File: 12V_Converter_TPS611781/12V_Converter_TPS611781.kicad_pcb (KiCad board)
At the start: 2 copper layers, 40.3 x 28.4 mm, 25 parts, among them M1 IQE050N08NM5CGSC, U1 LM51561HPWPR

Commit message: fix GND side of current sense probe and DRC issues
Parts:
- moved Cvcc1 0.06 mm to (77.8, 108.7)
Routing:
- net GND: track 58.7 -> 67.9 mm

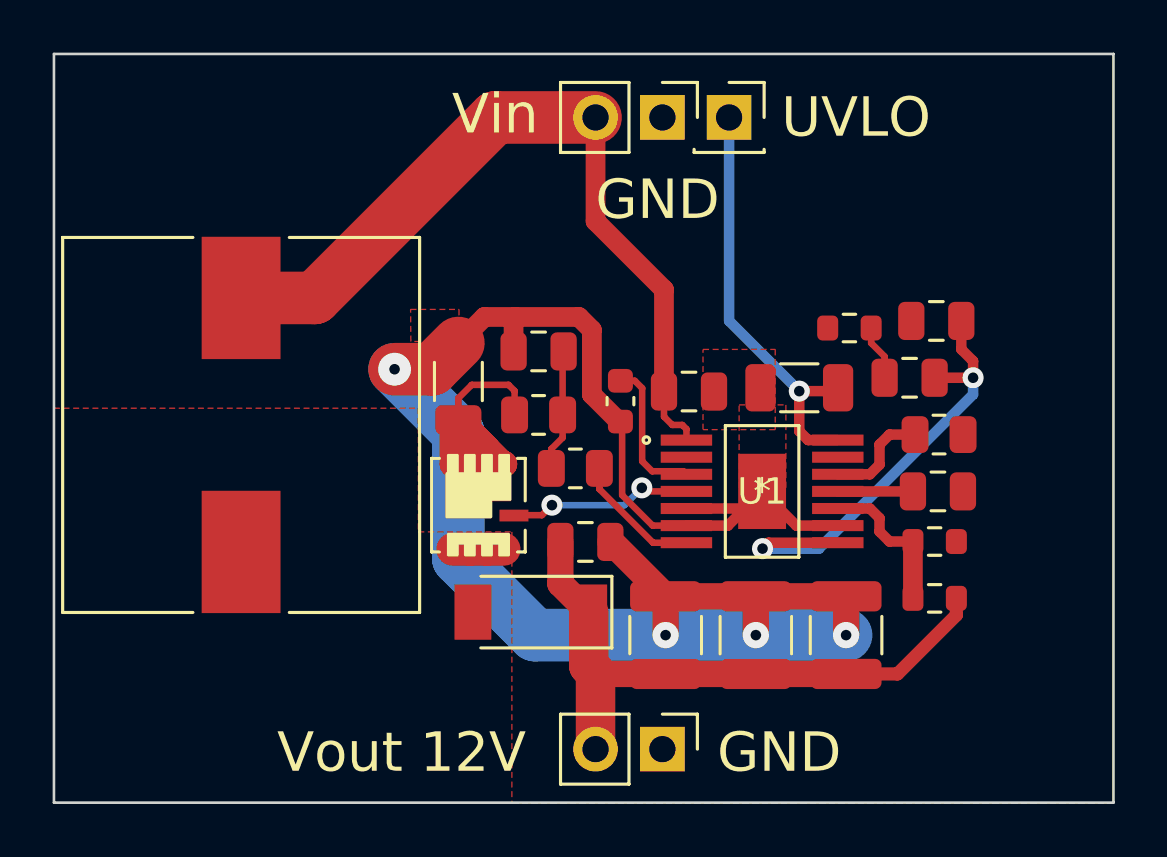
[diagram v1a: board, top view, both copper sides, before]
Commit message: improve thermals
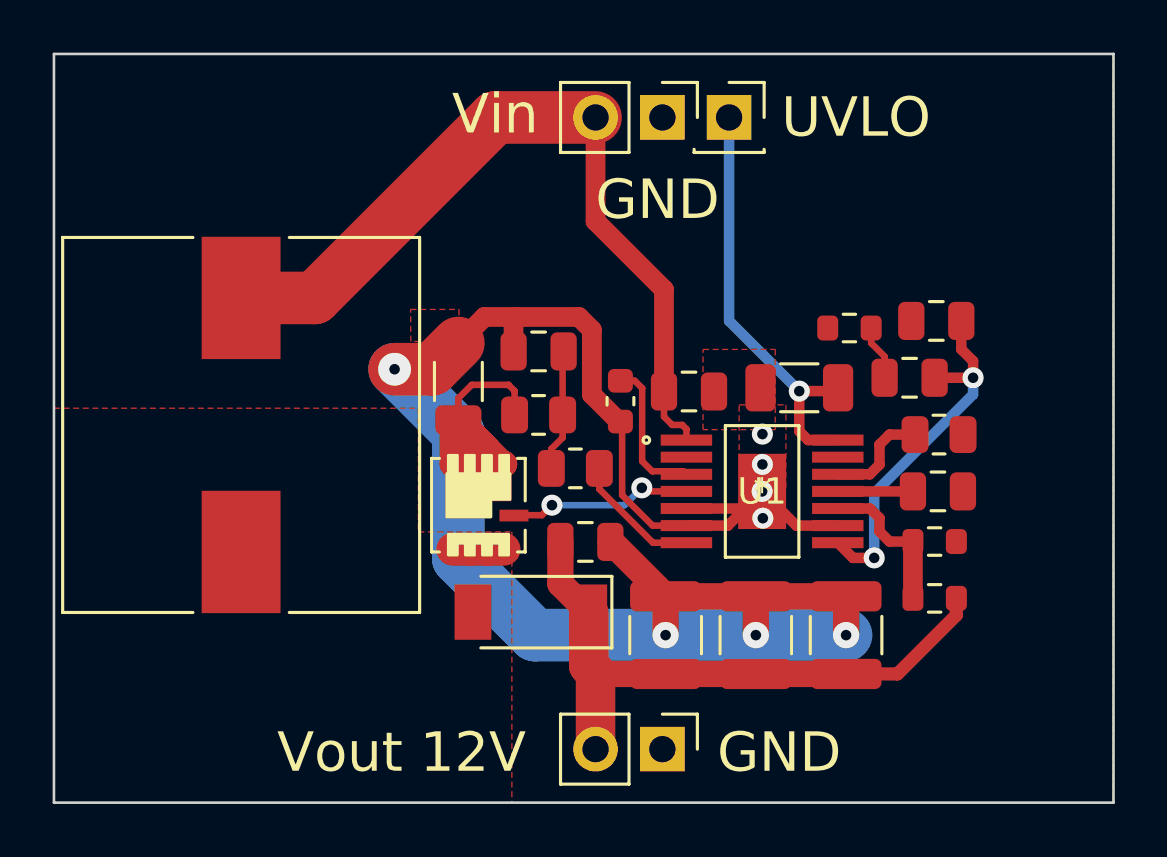
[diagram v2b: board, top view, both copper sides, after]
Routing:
- net Net-(Ccomp1-Pad2): track 17.8 -> 13.8 mm
- net GND: vias 4 -> 8
- added copper zone on B.Cu, net GND
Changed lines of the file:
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@@
   (via (at 79.501742 117.586999) (size 1) (drill 0.4) (layers "F.Cu" "B.Cu") (net 2))
   (via (at 86.359742 117.586999) (size 1) (drill 0.4) (layers "F.Cu" "B.Cu") (net 2))
+  (via (at 83.180652 109.949288) (size 0.8) (drill 0.4) (layers "F.Cu" "B.Cu") (free) (net 2))
+  (via (at 83.180652 111.10072) (size 0.8) (drill 0.4) (layers "F.Cu" "B.Cu") (net 2))
+  (via (at 83.169692 112.125999) (size 0.8) (drill 0.4) (layers "F.Cu" "B.Cu") (net 2))
+  (via (at 83.197152 113.145694) (size 0.8) (drill 0.4) (layers "F.Cu" "B.Cu") (net 2))
   (via (at 82.930742 117.586999) (size 1) (drill 0.4) (layers "F.Cu" "B.Cu") (net 2))
   (segment (start 71.628 109.90773) (end 71.628 114.681) (width 2) (layer "B.Cu") (net 2))
@@
   (segment (start 91.185742 107.807999) (end 89.722742 107.807999) (width 0.4) (layer "F.Cu") (net 4))
   (segment (start 90.738742 106.725999) (end 90.738742 105.648999) (width 0.4) (layer "F.Cu") (net 4))
-  (segment (start 83.409 114.076) (end 86.045076 114.076) (width 0.4) (layer "F.Cu") (net 4))
+  (segment (start 86.621442 114.652366) (end 86.045076 114.076) (width 0.4) (layer "F.Cu") (net 4))
+  (segment (start 87.428364 114.652366) (end 86.621442 114.652366) (width 0.4) (layer "F.Cu") (net 4))
   (segment (start 91.185742 107.172999) (end 90.738742 106.725999) (width 0.4) (layer "F.Cu") (net 4))
-  (segment (start 83.185 114.3) (end 83.409 114.076) (width 0.4) (layer "F.Cu") (net 4))
   (segment (start 91.185742 107.807999) (end 91.185742 107.172999) (width 0.4) (layer "F.Cu") (net 4))
   (via (at 91.185742 107.807999) (size 0.8) (drill 0.4) (layers "F.Cu" "B.Cu") (net 4))
-  (via (at 83.185 114.3) (size 0.8) (drill 0.4) (layers "F.Cu" "B.Cu") (net 4))
-  (segment (start 83.185 114.3) (end 85.328741 114.3) (width 0.4) (layer "B.Cu") (net 4))
-  (segment (start 85.328741 114.3) (end 91.185742 108.442999) (width 0.4) (layer "B.Cu") (net 4))
+  (via (at 87.428364 114.652366) (size 0.8) (drill 0.4) (layers "F.Cu" "B.Cu") (net 4))
   (segment (start 91.185742 108.442999) (end 91.185742 107.807999) (width 0.4) (layer "B.Cu") (net 4))
+  (segment (start 87.428364 114.652366) (end 87.428364 112.200377) (width 0.4) (layer "B.Cu") (net 4))
+  (segment (start 87.428364 112.200377) (end 91.185742 108.442999) (width 0.4) (layer "B.Cu") (net 4))
   (segment (start 75.5885 110.0855) (end 75.1605 110.5135) (width 0.25) (layer "F.Cu") (net 5))
   (segment (start 75.5885 106.8445) (end 75.626 106.807) (width 0.25) (layer "F.Cu") (net 5))
@@
     )
   )
-  (zone (net 2) (net_name "GND") (layer "F.Cu") (hatch edge 0.508)
+  (zone (net 0) (net_name "") (layer "F.Cu") (hatch edge 0.508)
+    (connect_pads (clearance 0))
+    (min_thickness 0.254)
+    (keepout (tracks allowed) (vias allowed) (pads allowed ) (copperpour not_allowed) (footprints allowed))
+    (fill (thermal_gap 0.508) (thermal_bridge_width 0.508))
+    (polygon
+      (pts
+        (xy 84.791964 114.32167)
+        (xy 81.48088 114.32167)
+        (xy 81.479963 113.854158)
+        (xy 84.791964 113.852325)
+      )
+    )
+  )
+  (zone (net 2) (net_name "GND") (layers F&B.Cu) (hatch edge 0.508)
     (connect_pads (clearance 0))
     (min_thickness 0.254) (filled_areas_thickness no)
@@
       )
     )
+  )
+  (zone (net 0) (net_name "") (layer "B.Cu") (hatch edge 0.508)
+    (connect_pads (clearance 0))
+    (min_thickness 0.254)
+    (keepout (tracks allowed) (vias allowed) (pads allowed ) (copperpour not_allowed) (footprints allowed))
+    (fill (thermal_gap 0.508) (thermal_bridge_width 0.508))
+    (polygon
+      (pts
+        (xy 93.621833 115.522798)
+        (xy 87.713017 115.524847)
+        (xy 79.121509 115.524847)
+        (xy 79.15252 102.277956)
+        (xy 81.752853 102.276233)
+        (xy 81.752853 102.573377)
+        (xy 81.75475 102.720396)
+        (xy 79.513223 102.721672)
+        (xy 79.506331 115.159188)
+        (xy 93.282151 115.159188)
+        (xy 93.282151 102.714346)
+        (xy 82.083949 102.714346)
+        (xy 82.083949 102.274495)
+        (xy 93.621833 102.274495)
+      )
+    )
